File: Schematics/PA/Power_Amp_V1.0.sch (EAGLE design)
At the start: 123 parts, among them J1 4_PIN_AMPCONN, U1 LME49830, U2 LME49830, U3 LME49830, X1 5566-4

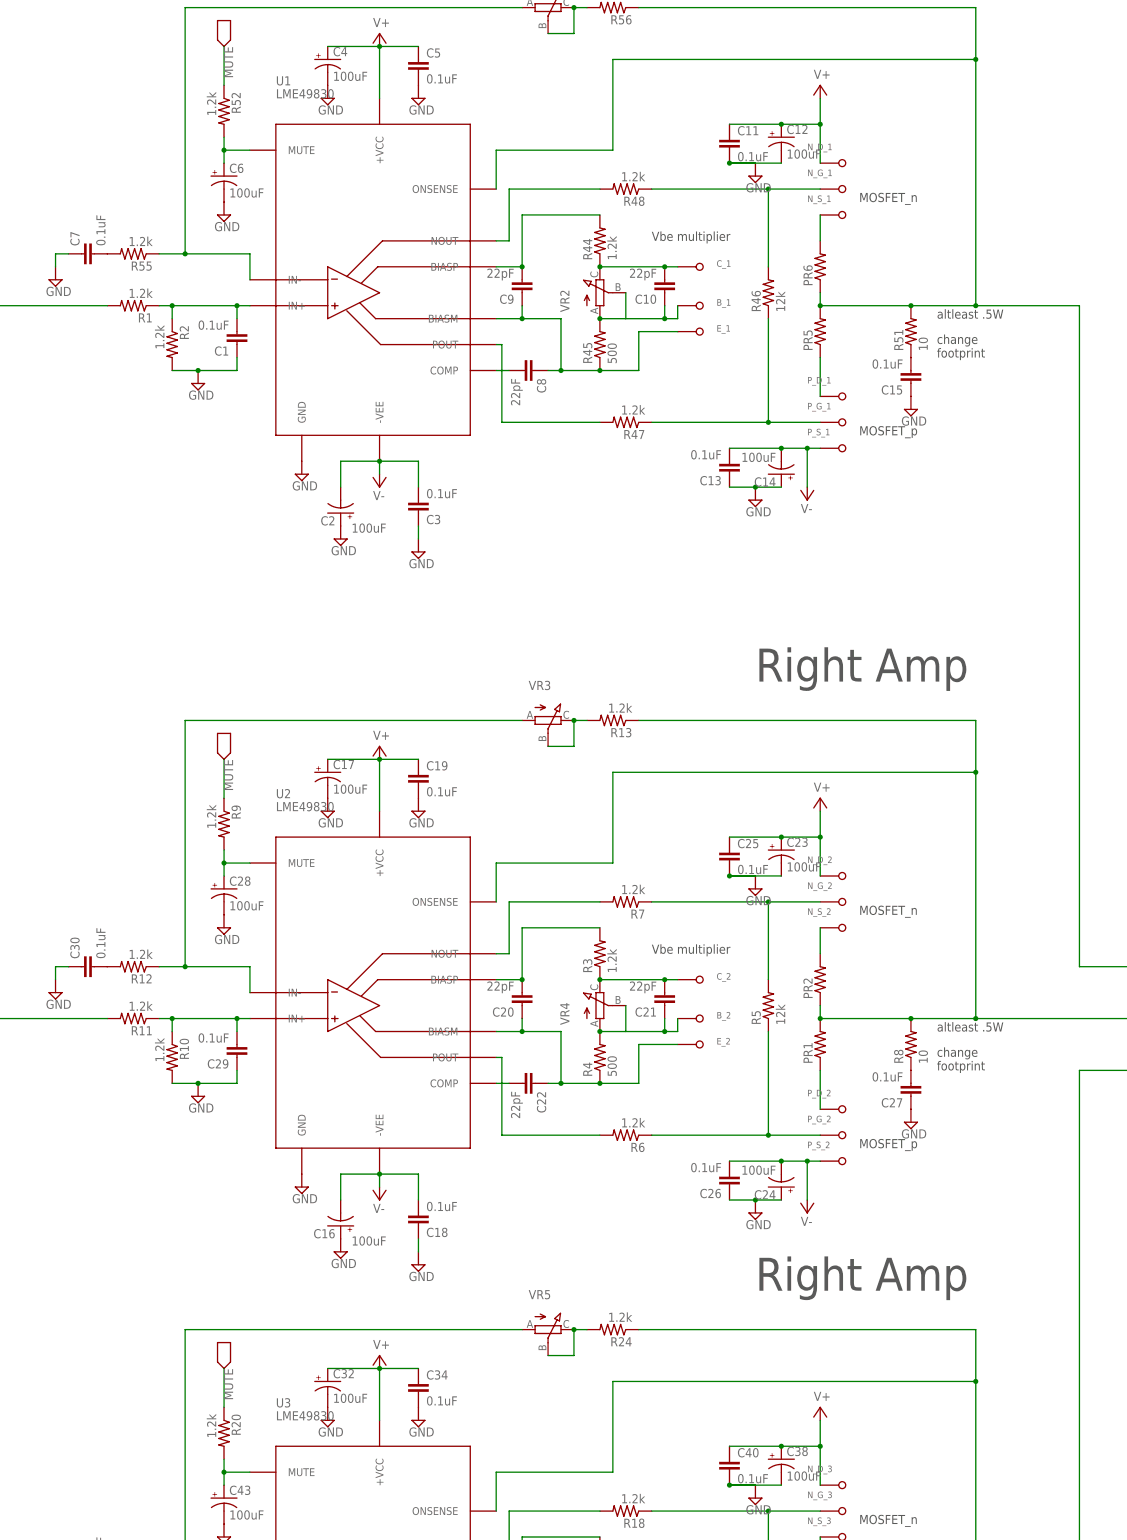
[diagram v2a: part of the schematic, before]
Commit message: added part values to PA from breadboard prototype
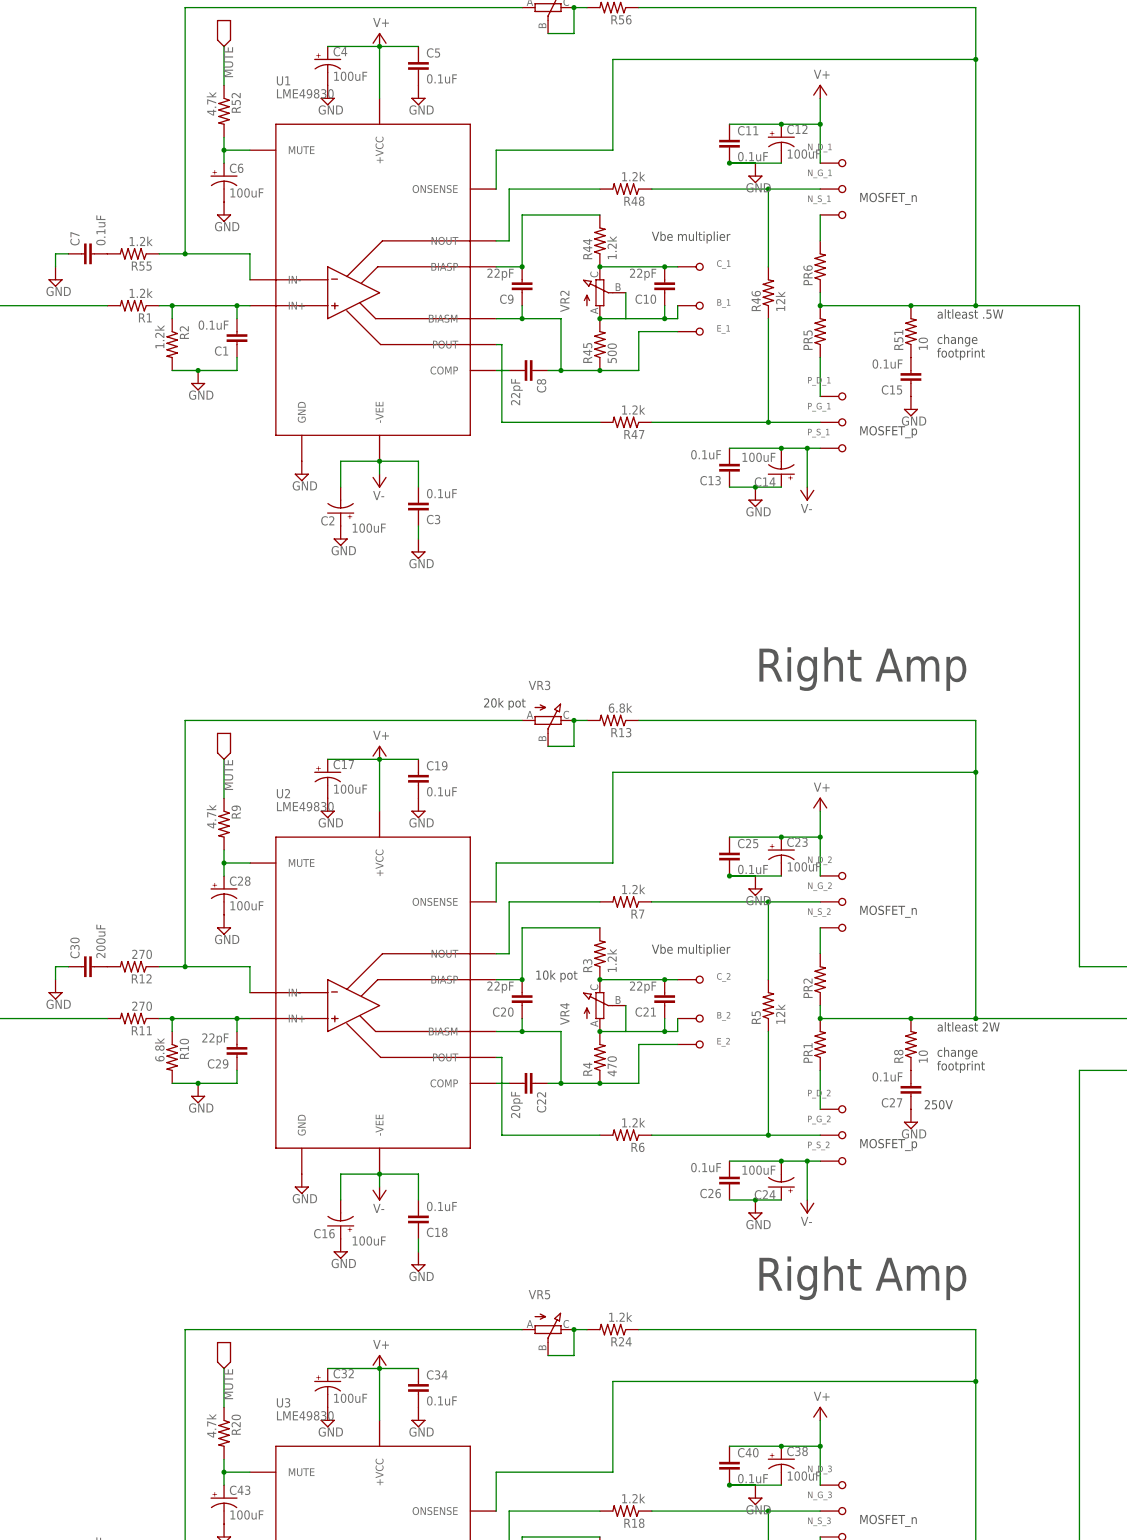
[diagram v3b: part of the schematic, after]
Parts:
- C22: value 22pF -> 20pF
- C29: value 0.1uF -> 22pF
- C30: value 0.1uF -> 200uF
- R10, R13: value 1.2k -> 6.8k
- R11, R12: value 1.2k -> 270
- R20, R52, R9: value 1.2k -> 4.7k
- R4: value 500 -> 470
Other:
- note added: "10k pot"
- note added: "20k pot"
- note added: "250V"
- note added: "altleast 2W"
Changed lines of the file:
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@@
 <?xml version="1.0" encoding="utf-8"?>
 <!DOCTYPE eagle SYSTEM "eagle.dtd">
-<eagle version="7.4.0">
+<eagle version="6.5.0">
 <drawing>
 <settings>
@@
 <setting verticaltext="up"/>
 </settings>
-<grid distance="0.1" unitdist="inch" unit="inch" style="lines" multiple="1" display="yes" altdistance="0.01" altunitdist="inch" altunit="inch"/>
+<grid distance="0.1" unitdist="inch" unit="inch" style="lines" multiple="1" display="no" altdistance="0.01" altunitdist="inch" altunit="inch"/>
 <layers>
 <layer number="1" name="Top" color="4" fill="1" visible="no" active="no"/>
@@
 <part name="C15" library="rcl" deviceset="C-EU" device="050-024X044" value="0.1uF"/>
 <part name="C6" library="rcl" deviceset="CPOL-US" device="E2.5-6" value="100uF"/>
-<part name="R52" library="rcl" deviceset="R-US_" device="0204/2V" value="1.2k"/>
+<part name="R52" library="rcl" deviceset="R-US_" device="0204/2V" value="4.7k"/>
 <part name="GND22" library="supply2" deviceset="GND" device=""/>
 <part name="GND23" library="supply2" deviceset="GND" device=""/>
@@
 <part name="C21" library="rcl" deviceset="C-EU" device="050-024X044" value="22pF"/>
 <part name="R3" library="rcl" deviceset="R-US_" device="0204/2V" value="1.2k"/>
-<part name="R4" library="rcl" deviceset="R-US_" device="0204/2V" value="500"/>
-<part name="C22" library="rcl" deviceset="C-EU" device="050-024X044" value="22pF"/>
+<part name="R4" library="rcl" deviceset="R-US_" device="0204/2V" value="470"/>
+<part name="C22" library="rcl" deviceset="C-EU" device="050-024X044" value="20pF"/>
 <part name="R5" library="rcl" deviceset="R-US_" device="0204/2V" value="12k"/>
 <part name="R6" library="rcl" deviceset="R-US_" device="0204/2V" value="1.2k"/>
@@
 <part name="C27" library="rcl" deviceset="C-EU" device="050-024X044" value="0.1uF"/>
 <part name="C28" library="rcl" deviceset="CPOL-US" device="E2.5-6" value="100uF"/>
-<part name="R9" library="rcl" deviceset="R-US_" device="0204/2V" value="1.2k"/>
+<part name="R9" library="rcl" deviceset="R-US_" device="0204/2V" value="4.7k"/>
 <part name="GND2" library="supply2" deviceset="GND" device=""/>
 <part name="GND3" library="supply2" deviceset="GND" device=""/>
@@
 <part name="SUPPLY6" library="supply2" deviceset="GND" device=""/>
 <part name="SUPPLY7" library="supply2" deviceset="V-" device=""/>
-<part name="C29" library="rcl" deviceset="C-EU" device="050-024X044" value="0.1uF"/>
-<part name="R10" library="rcl" deviceset="R-US_" device="0204/2V" value="1.2k"/>
+<part name="C29" library="rcl" deviceset="C-EU" device="050-024X044" value="22pF"/>
+<part name="R10" library="rcl" deviceset="R-US_" device="0204/2V" value="6.8k"/>
 <part name="GND6" library="supply2" deviceset="GND" device=""/>
-<part name="R11" library="rcl" deviceset="R-US_" device="0204/2V" value="1.2k"/>
-<part name="R12" library="rcl" deviceset="R-US_" device="0204/2V" value="1.2k"/>
-<part name="C30" library="rcl" deviceset="C-EU" device="050-024X044" value="0.1uF"/>
+<part name="R11" library="rcl" deviceset="R-US_" device="0204/2V" value="270"/>
+<part name="R12" library="rcl" deviceset="R-US_" device="0204/2V" value="270"/>
+<part name="C30" library="rcl" deviceset="C-EU" device="050-024X044" value="200uF"/>
 <part name="GND7" library="supply2" deviceset="GND" device=""/>
-<part name="R13" library="rcl" deviceset="R-US_" device="0204/2V" value="1.2k"/>
+<part name="R13" library="rcl" deviceset="R-US_" device="0204/2V" value="6.8k"/>
 <part name="GND8" library="supply2" deviceset="GND" device=""/>
 <part name="GND9" library="supply2" deviceset="GND" device=""/>
 <part name="SUPPLY8" library="supply2" deviceset="V-" device=""/>
 <part name="GND10" library="supply2" deviceset="GND" device=""/>
-<part name="P+3" library="supply2" deviceset="V+" device=""/>
+<part name="P+3" library="supply2" deviceset="V+" device="" value="V+"/>
 <part name="PR1" library="Power Resistors" deviceset="SQM" device=""/>
 <part name="PR2" library="Power Resistors" deviceset="SQM" device=""/>
@@
 <part name="C42" library="rcl" deviceset="C-EU" device="050-024X044" value="0.1uF"/>
 <part name="C43" library="rcl" deviceset="CPOL-US" device="E2.5-6" value="100uF"/>
-<part name="R20" library="rcl" deviceset="R-US_" device="0204/2V" value="1.2k"/>
+<part name="R20" library="rcl" deviceset="R-US_" device="0204/2V" value="4.7k"/>
 <part name="GND11" library="supply2" deviceset="GND" device=""/>
 <part name="GND12" library="supply2" deviceset="GND" device=""/>
@@
 footprint</text>
 <text x="434.34" y="299.72" size="6.4516" layer="97">Right Amp</text>
-<text x="469.9" y="231.14" size="1.778" layer="97">altleast .5W</text>
+<text x="469.9" y="231.14" size="1.778" layer="97">altleast 2W</text>
 <text x="414.02" y="127" size="1.778" layer="97">Vbe multiplier</text>
 <text x="454.66" y="134.62" size="1.778" layer="97">MOSFET_n</text>
@@
 <text x="434.34" y="180.34" size="6.4516" layer="97">Right Amp</text>
 <text x="469.9" y="111.76" size="1.778" layer="97">altleast .5W</text>
+<text x="381" y="294.64" size="1.778" layer="97">20k pot</text>
+<text x="391.16" y="241.3" size="1.778" layer="97">10k pot</text>
+<text x="467.36" y="215.9" size="1.778" layer="97">250V</text>
 </plain>
 <instances>

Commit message: updated my PA schematic
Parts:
- removed B_1, B_2, B_3, C_1, C_2, C_3, E_1, E_2, E_3, N_D_1, N_D_2, N_D_3, N_G_1, N_G_2, N_G_3, N_S_1, N_S_2, N_S_3, P_D_1, P_D_2, P_D_3, P_G_1, P_G_2, P_G_3, P_S_1, P_S_2, P_S_3: (no value), Amplifier_Parts:18AWG_HOLE
- added J10, J2, J3, J4, J5, J6, J7, J8, J9: OSTVN03A150, Amplifier_Parts:OSTVN03A150
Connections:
- net N$1: no longer C_2.>NAME
- net N$11: now also J5.3; no longer N_S_2.>NAME
- net N$110: now also J4.1; no longer P_D_1.>NAME
- net N$2: now also J6.2; no longer B_2.>NAME
- net N$22: now also J7.1; no longer P_D_2.>NAME
- net N$23: no longer C_3.>NAME
- net N$24: now also J9.2; no longer B_3.>NAME
- net N$26: now also J9.3; no longer E_3.>NAME
- net N$30: now also J8.2; no longer N_G_3.>NAME
- net N$32: now also J10.2; no longer P_G_3.>NAME
- net N$33: now also J8.3; no longer N_S_3.>NAME
- net N$45: now also J10.1; no longer P_D_3.>NAME
- net N$5: now also J6.3; no longer E_2.>NAME
- net N$65: no longer C_1.>NAME
- net N$67: now also J3.3; no longer E_1.>NAME
- net N$68: now also J3.2; no longer B_1.>NAME
- net N$72: now also J2.2; no longer N_G_1.>NAME
- net N$73: now also J4.2; no longer P_G_1.>NAME
- net N$74: now also J2.3; no longer N_S_1.>NAME
- net N$8: now also J5.2; no longer N_G_2.>NAME
- net N$9: now also J7.2; no longer P_G_2.>NAME
- net V+: now also J2.1, J5.1, J8.1; no longer N_D_1.>NAME, N_D_2.>NAME, N_D_3.>NAME
- net V-: now also J10.3, J4.3, J7.3; no longer P_S_1.>NAME, P_S_2.>NAME, P_S_3.>NAME

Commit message: updated PA PCB
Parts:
- removed J2, J3, J4: OSTVN03A150, Amplifier_Parts:OSTVN03A150
- removed X1: 5566-4, con-molex:5566-4
- added J11: SCREW_TERMINAL_4, Amplifier_Parts:SCREW_TERMINAL_4
- added J12, J13, J14: 1725724, Amplifier_Parts:1725724
- C28, C43, C6: device rcl:CPOL-USE2.5-6 -> rcl:C-EU050-024X044
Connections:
- net N$65 renamed R_VBE_C
- removed net N$67: C8.1, C9.1, J3.3, R45.1, U1.BIASM
- removed net N$68: C10.1, J3.2, R45.2, VR2.A, VR2.B
- removed net N$72: J2.2, R46.2, R48.1
- removed net N$74: J2.3, PR6.2
- new net N$29: J12.4
- new net N$34: J12.5
- new net N$44: J12.6
- new net R_NMOS_G: J12.2, R46.2, R48.1
- new net R_NMOS_S: J12.3, PR6.2
- new net R_PMOS_G: J12.7, J12.8
- new net R_VBE_B: C10.1, R45.2, VR2.A, VR2.B
- new net R_VBE_E: C8.1, C9.1, R45.1, U1.BIASM
- net GND: now also C28.2, C43.2, C6.2, J11.S1; no longer C28.-, C43.-, C6.-, X1-2.S
- net MUTE: now also J11.S2; no longer X1-1.S
- net N$1: now also J6.1
- net N$110: no longer J4.1
- net N$14: now also C28.1; no longer C28.+
- net N$23: now also J9.1
- net N$37: now also C43.1; no longer C43.+
- net N$73: no longer J4.2
- net N$85: now also C6.1; no longer C6.+
- net V+: now also J11.S4, J12.1; no longer J2.1, X1-4.S
- net V-: now also J11.S3, J12.9; no longer J4.3, X1-3.S
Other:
- note added: "Bass Amp"
- note added: "Left Amp"
- moved on the sheet: C11, C12, C13, C14

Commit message: updated PA
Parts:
- removed J10, J5, J6, J7, J8, J9: OSTVN03A150, Amplifier_Parts:OSTVN03A150
- PR1, PR2, PR3, PR4, PR5, PR6: device Power Resistors:SQM -> rcl:R-US_0617/5V
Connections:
- removed net N$1: C21.2, J6.1, R3.1, VR4.C
- removed net N$11: J5.3, PR2.2
- removed net N$110: PR5.1
- removed net N$2: C21.1, J6.2, R4.2, VR4.A, VR4.B
- removed net N$22: J7.1, PR1.1
- removed net N$23: C36.2, J9.1, R14.1, VR6.C
- removed net N$24: C36.1, J9.2, R15.2, VR6.A, VR6.B
- removed net N$26: C35.1, C37.1, J9.3, R15.1, U3.BIASM
- removed net N$29: J12.4
- removed net N$30: J8.2, R16.2, R18.1
- removed net N$32: J10.2, R16.1, R17.1
- removed net N$33: J8.3, PR4.2
- removed net N$34: J12.5
- removed net N$44: J12.6
- removed net N$45: J10.1, PR3.1
- removed net N$5: C20.1, C22.1, J6.3, R4.1, U2.BIASM
- removed net N$73: R46.1, R47.1
- removed net N$8: J5.2, R5.2, R7.1
- removed net N$9: J7.2, R5.1, R6.1
- new net B_NMOS_G: J13.2, R5.2, R7.1
- new net B_NMOS_S: J13.3, PR2.2
- new net B_PMOS_G: J13.8, R5.1, R6.1
- new net B_PMOS_S: J13.7, PR1.1
- new net B_VBE_B: C21.1, J13.5, R4.2, VR4.A, VR4.B
- new net B_VBE_C: C21.2, J13.6, R3.1, VR4.C
- new net B_VBE_E: C20.1, C22.1, J13.4, R4.1, U2.BIASM
- new net L_NMOS_G: J14.2, R16.2, R18.1
- new net L_NMOS_S: J14.3, PR4.2
- new net L_PMOS_G: J14.8, R16.1, R17.1
- new net L_PMOS_S: J14.7, PR3.1
- new net L_VBE_B: C36.1, J14.5, R15.2, VR6.A, VR6.B
- new net L_VBE_C: C36.2, J14.6, R14.1, VR6.C
- new net L_VBE_E: C35.1, C37.1, J14.4, R15.1, U3.BIASM
- new net R_PMOS_S: J12.7, PR5.1
- net R_PMOS_G: now also R46.1, R47.1; no longer J12.7
- net R_VBE_B: now also J12.5
- net R_VBE_C: now also J12.6
- net R_VBE_E: now also J12.4
- net V+: now also J13.1, J14.1; no longer J5.1, J8.1
- net V-: now also J13.9, J14.9; no longer J10.3, J7.3
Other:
- moved on the sheet: C23, C24, C25, C26, C38, C39, C40, C41, R6
